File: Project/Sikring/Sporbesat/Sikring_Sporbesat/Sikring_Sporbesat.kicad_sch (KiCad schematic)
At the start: 0 parts

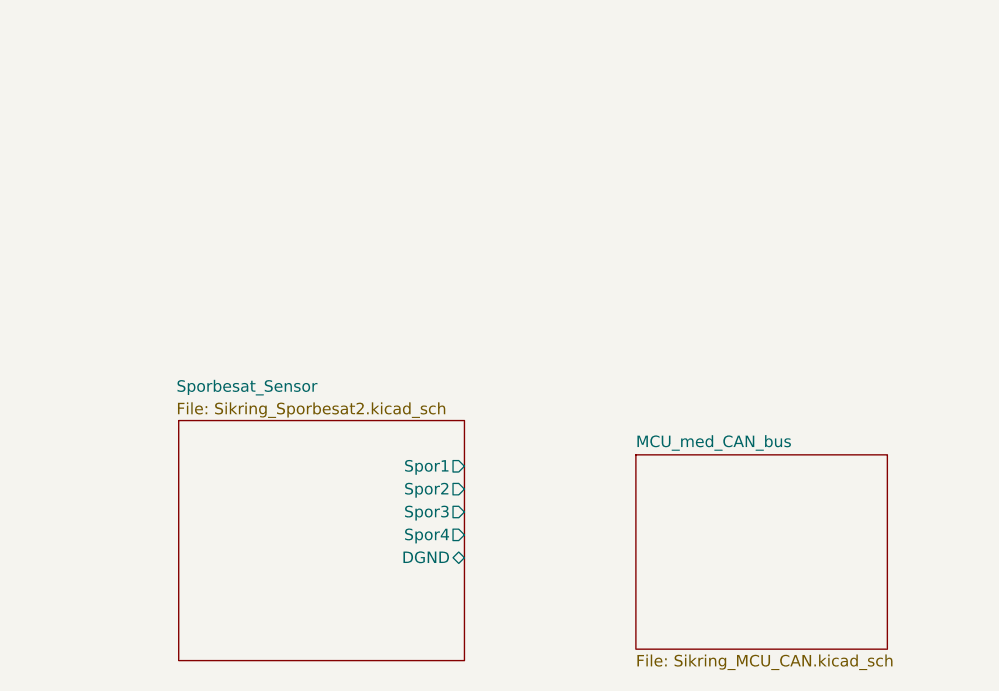
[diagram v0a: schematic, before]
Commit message: pcb på vej
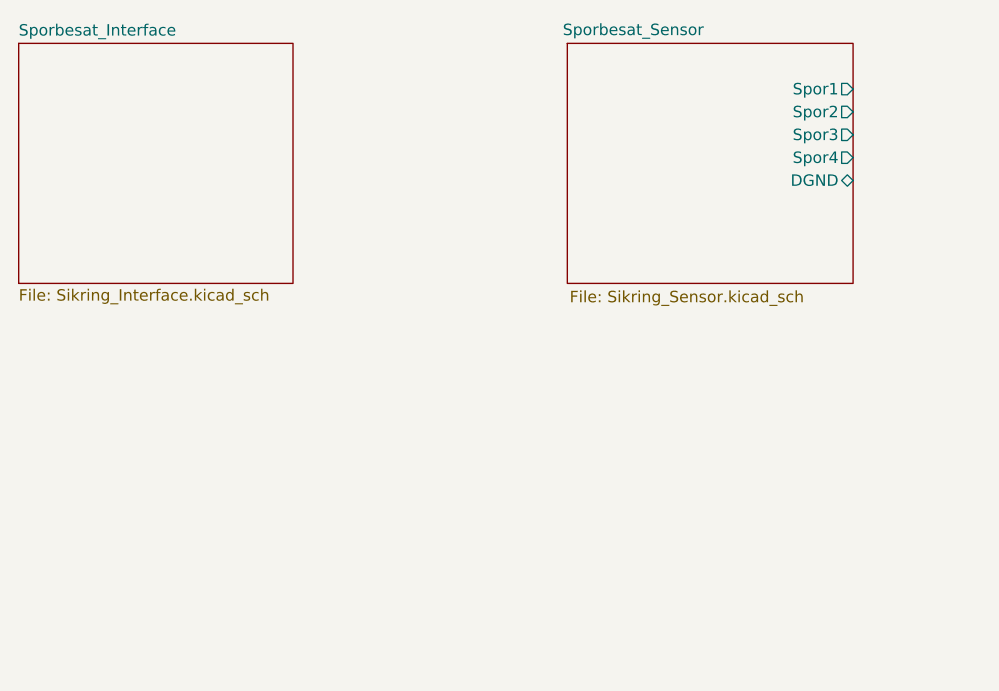
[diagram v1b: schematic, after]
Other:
- removed sheet MCU_med_CAN_bus
- added sheet Sporbesat_Interface (Sikring_Interface.kicad_sch)
- sheet Sporbesat_Sensor: file Sikring_Sporbesat2.kicad_sch -> Sikring_Sensor.kicad_sch
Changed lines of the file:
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@@
 	(paper "A4")
 	(sheet
-		(at 107.95 73.66)
-		(size 27.94 21.59)
+		(at 39.37 27.94)
+		(size 30.48 26.67)
 		(exclude_from_sim no)
 		(in_bom yes)
@@
 			(color 0 0 0 0)
 		)
-		(property "Sheetname" "MCU_med_CAN_bus"
-			(at 107.95 72.9484 0)
-			(show_name no)
+		(property "Sheetname" "Sporbesat_Interface"
+			(at 39.37 27.2284 0)
+			(show_name yes)
 			(do_not_autoplace no)
 			(effects
@@
 			)
 		)
-		(property "Sheetfile" "Sikring_MCU_CAN.kicad_sch"
-			(at 107.95 95.8346 0)
-			(show_name no)
+		(property "Sheetfile" "Sikring_Interface.kicad_sch"
+			(at 39.37 55.1946 0)
+			(show_name yes)
 			(do_not_autoplace no)
 			(effects
@@
 			(project "Sikring_Sporbesat"
 				(path "/15e6cd25-56b2-4983-bc16-60cbc7cb2d3a"
-					(page "3")
+					(page "2")
 				)
 			)
@@
 	)
 	(sheet
-		(at 57.15 69.85)
+		(at 100.33 27.94)
 		(size 31.75 26.67)
 		(exclude_from_sim no)
@@
 		)
 		(property "Sheetname" "Sporbesat_Sensor"
-			(at 56.896 66.802 0)
+			(at 99.822 27.178 0)
 			(show_name no)
 			(do_not_autoplace no)
@@
 			)
 		)
-		(property "Sheetfile" "Sikring_Sporbesat2.kicad_sch"
-			(at 56.896 67.818 0)
+		(property "Sheetfile" "Sikring_Sensor.kicad_sch"
+			(at 100.584 55.372 0)
 			(show_name no)
 			(do_not_autoplace no)
@@
 		)
 		(pin "DGND" bidirectional
-			(at 88.9 85.09 0)
+			(at 132.08 43.18 0)
 			(effects
 				(font
@@
 		)
 		(pin "Spor1" output
-			(at 88.9 74.93 0)
+			(at 132.08 33.02 0)
 			(effects
 				(font
@@
 		)
 		(pin "Spor2" output
-			(at 88.9 77.47 0)
+			(at 132.08 35.56 0)
 			(effects
 				(font
@@
 		)
 		(pin "Spor3" output
-			(at 88.9 80.01 0)
+			(at 132.08 38.1 0)
 			(effects
 				(font
@@
 		)
 		(pin "Spor4" output
-			(at 88.9 82.55 0)
+			(at 132.08 40.64 0)
 			(effects
 				(font
@@
 			(project "Sikring_Sporbesat"
 				(path "/15e6cd25-56b2-4983-bc16-60cbc7cb2d3a"
-					(page "2")
+					(page "3")
 				)
 			)
